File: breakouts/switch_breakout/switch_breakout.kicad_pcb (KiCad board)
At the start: 2 copper layers, 11 parts, among them P1 CONN_01X03, U1 CONN_SMA, U2 CONN_SMA, U3 PE42521, U4 CONN_SMA, U5 mounting_box

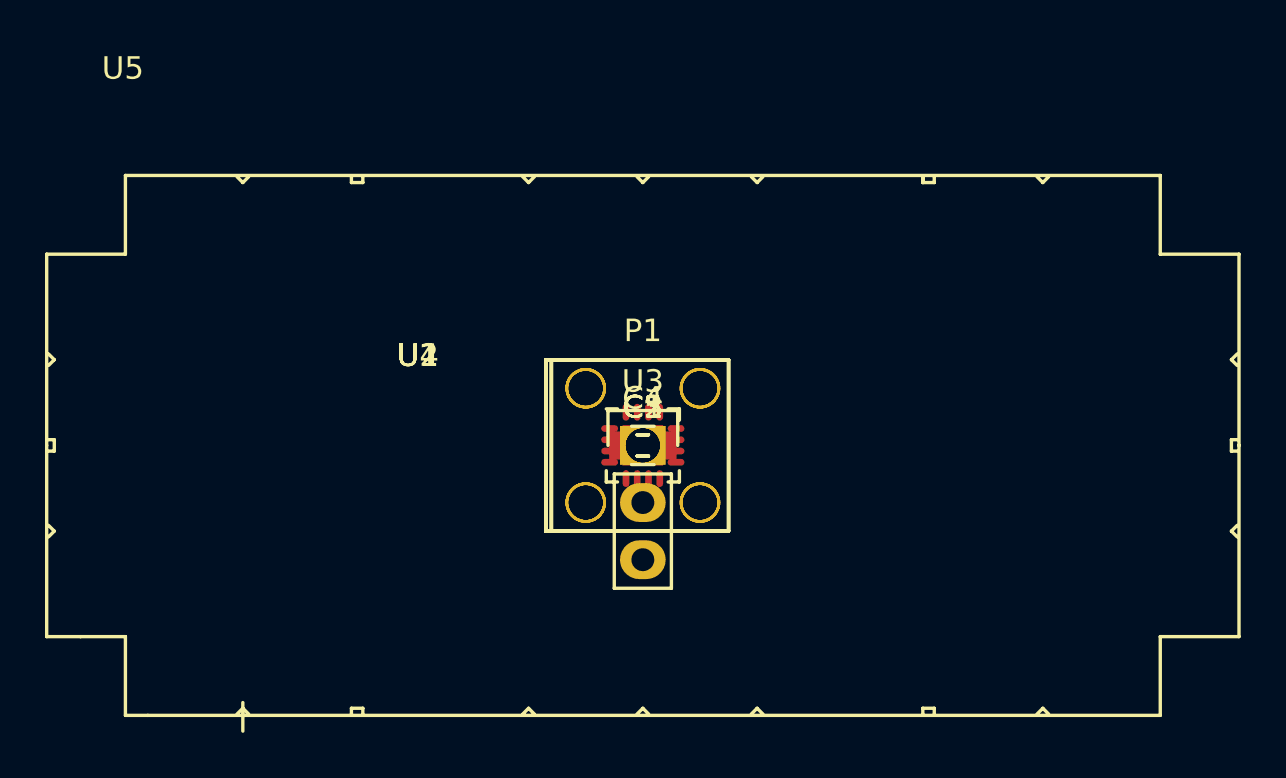
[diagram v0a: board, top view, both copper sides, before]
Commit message: layout of splitter, switch, and filter
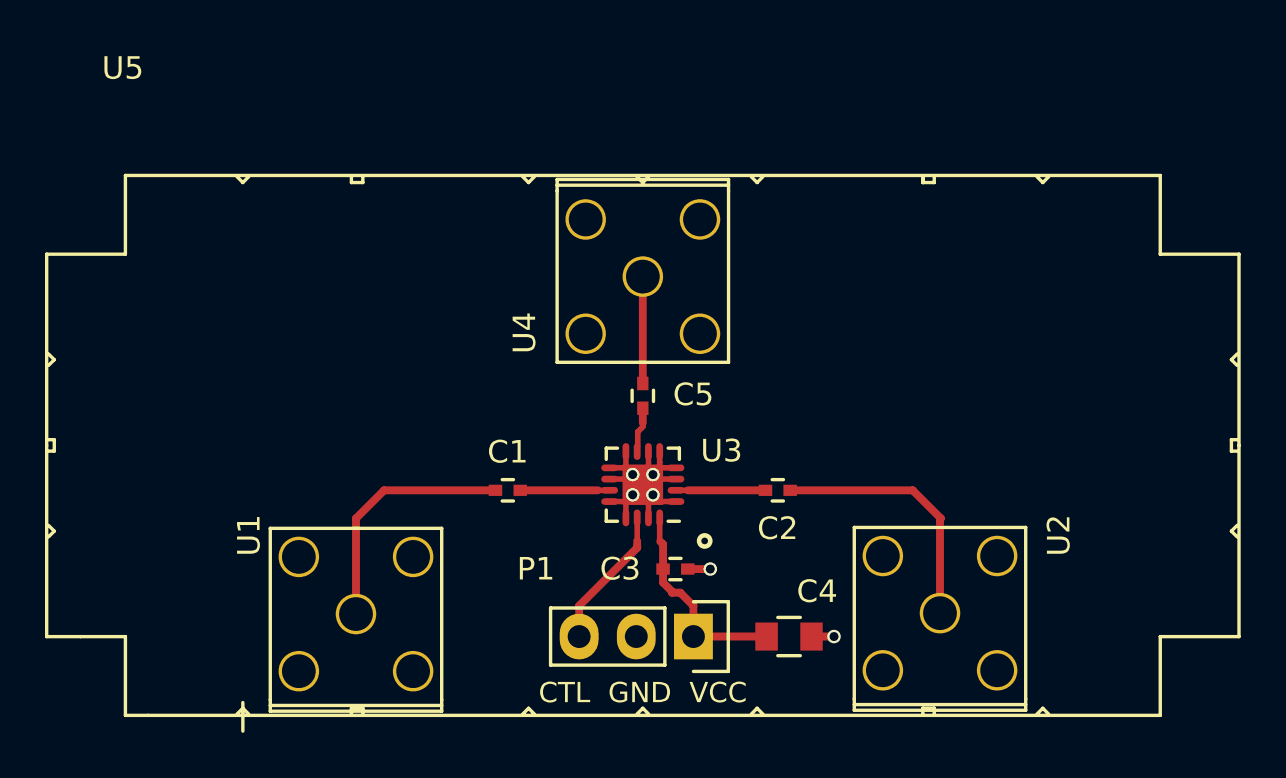
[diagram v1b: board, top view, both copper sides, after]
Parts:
- moved U2 15.2 mm to (161.7, 112.5), turned to 90 degrees
- moved U1 14.8 mm to (135.8, 112.5), turned to 90 degrees
- moved C4 10.7 mm to (155.0, 113.5)
- moved P1 8.79 mm to (150.8, 113.5), turned to 270 degrees
- moved U4 7.50 mm to (148.5, 97.5), turned to 270 degrees
- moved C1 6.32 mm to (142.5, 107.0)
- moved C2 6.32 mm to (154.5, 107.0), turned to 180 degrees
- moved C3 5.68 mm to (149.9, 110.5)
- moved C5 2.20 mm to (148.5, 102.8), turned to 270 degrees
- moved U3 1.75 mm to (148.5, 106.8), turned to 180 degrees
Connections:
- U3 pad 17: Net-(U3-Pad17) -> GND
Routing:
- net GND: track 0.00 -> 13.6 mm, vias 0 -> 6
- net Net-(C2-Pad1): track 0.00 -> 11.4 mm
- net Net-(C1-Pad1): track 0.00 -> 11.0 mm
- net Net-(C3-Pad1): track 0.00 -> 9.36 mm
- net Net-(P1-Pad3): track 0.00 -> 6.50 mm
- net Net-(C5-Pad1): track 0.00 -> 4.75 mm
- net Net-(C2-Pad2): track 0.00 -> 3.97 mm
- net Net-(C1-Pad2): track 0.00 -> 3.97 mm
- net Net-(C5-Pad2): track 0.00 -> 1.77 mm
- added copper zone on In1.Cu, net GND
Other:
- copper layers 2 -> 4
- board text added: "CTL GND VCC"

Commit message: started variable attenuator, revised synth, and added power splittert to detect board
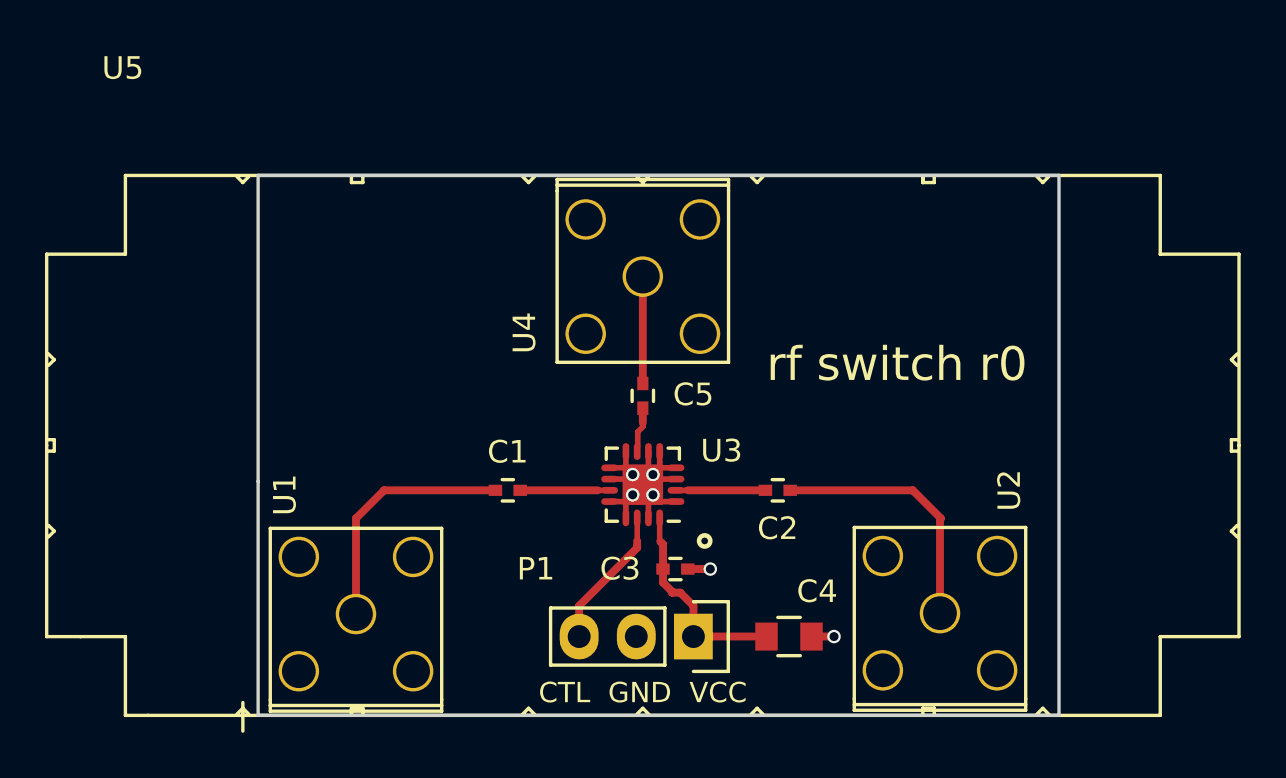
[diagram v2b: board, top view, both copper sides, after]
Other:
- board outline added: 35.6 x 24 mm
- board text added: "2016.03"
- board text added: "rf switch r0"
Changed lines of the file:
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@@
   (general
     (links 39)
-    (no_connects 39)
-    (area 0 0 0 0)
+    (no_connects 0)
+    (area 117.25 85.8446 178.250001 122.703571)
     (thickness 1.6)
-    (drawings 2)
+    (drawings 9)
     (tracks 63)
     (zones 0)
@@
   )
   (setup
-    (last_trace_width 0.35)
+    (last_trace_width 0.25)
     (user_trace_width 0.35)
     (trace_clearance 0.2)
@@
     (visible_elements FFFEFF7F)
     (pcbplotparams
-      (layerselection 0x00030_80000001)
+      (layerselection 0x010f0_80000007)
       (usegerberextensions false)
       (excludeedgelayer true)
@@
       (outputformat 1)
       (mirror false)
-      (drillshape 1)
+      (drillshape 0)
       (scaleselection 1)
-      (outputdirectory ""))
+      (outputdirectory gerbs/))
   )
   (net 0 "")
@@
   (module vna_footprints:732512200_SMA (layer F.Cu)
     (at 135.75 112.5 90)
-    (fp_text reference U1 (at 3.5 -4.75 90) (layer F.SilkS)
+    (fp_text reference U1 (at 5.3 -3.15 90) (layer F.SilkS)
       (effects (font (size 1 1) (thickness 0.15)))
     )
@@
   (module vna_footprints:732512200_SMA (layer F.Cu)
     (at 161.71 112.46 90)
-    (fp_text reference U2 (at 3.46 5.29 90) (layer F.SilkS)
+    (fp_text reference U2 (at 5.46 3.09 90) (layer F.SilkS)
       (effects (font (size 1 1) (thickness 0.15)))
     )
@@
       (net 6 GND))
   )
+  (gr_text "rf switch r0" (at 159.8 101.4) (layer F.SilkS)
+    (effects (font (size 1.5 1.5) (thickness 0.3)))
+  )
+  (gr_text 2016.03 (at 160 97) (layer B.SilkS)
+    (effects (font (size 1.5 1.5) (thickness 0.3)) (justify mirror))
+  )
+  (gr_line (start 167 117) (end 131.4 117) (layer Edge.Cuts) (width 0.15))
+  (gr_line (start 167 93) (end 167 117) (layer Edge.Cuts) (width 0.15))
+  (gr_line (start 131.4 93) (end 167 93) (layer Edge.Cuts) (width 0.15))
+  (gr_line (start 131.4 106.6) (end 131.4 93) (layer Edge.Cuts) (width 0.15))
+  (gr_line (start 131.4 117) (end 131.4 106.6) (layer Edge.Cuts) (width 0.15))
   (gr_text "CTL  GND  VCC" (at 148.5 116) (layer F.SilkS)
     (effects (font (size 0.9 0.9) (thickness 0.225)))

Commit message: trimmed ground plane on some breakouts so it doesn't disappear during panelization..
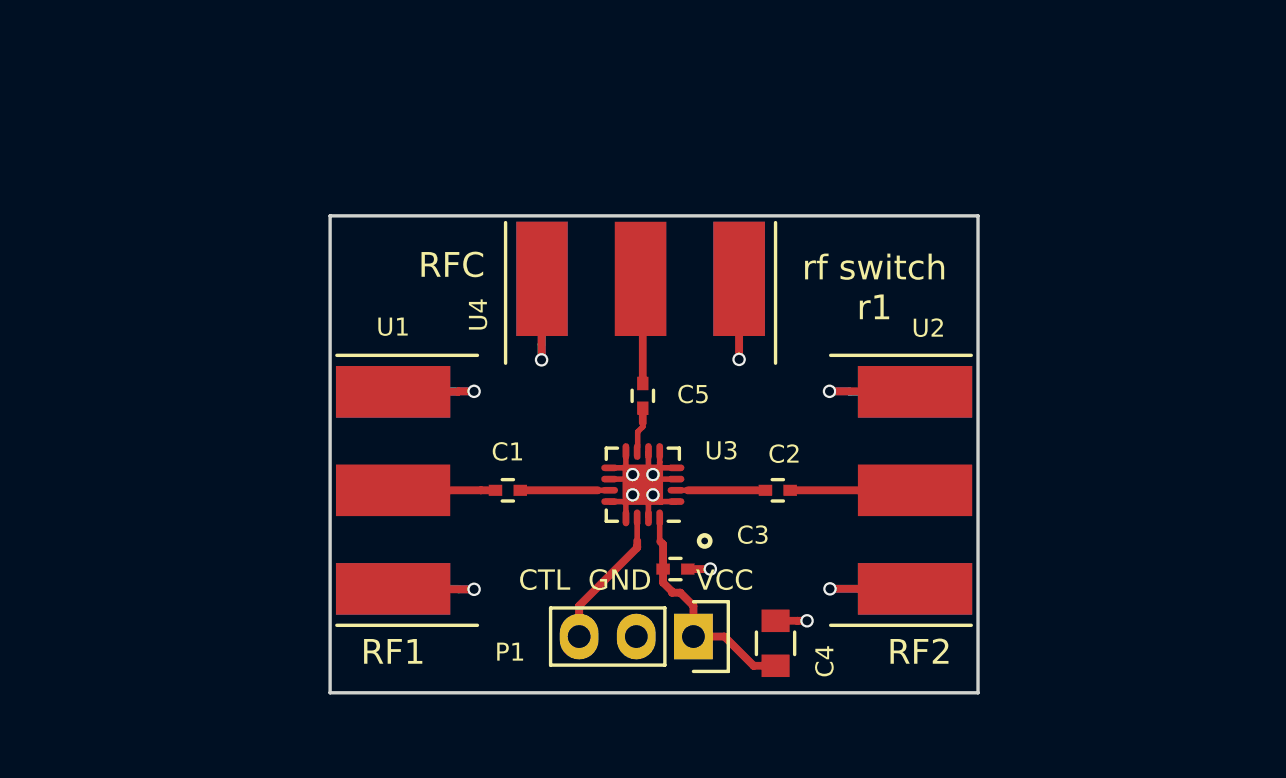
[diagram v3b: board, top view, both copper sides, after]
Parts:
- removed U5: mounting_box, vna_footprints:POMONA_2400BOX
- C1, C2, C3, C5: value C_Small -> 100 pF
- C4: value C_Small -> 10 uF
- U1, U2, U4: footprint vna_footprints:732512200_SMA -> vna_footprints:732511150_sma
- moved U1 5.74 mm to (137.4, 107.0), turned to 270 degrees
- moved U2 5.57 mm to (160.6, 107.0)
- moved C4 0.67 mm to (154.4, 113.8), turned to 90 degrees
- moved U4 0.14 mm to (148.4, 97.6), turned to 180 degrees
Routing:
- net GND: track 13.6 -> 54.4 mm, vias 6 -> 12
- net Net-(C1-Pad1): track 11.0 -> 4.55 mm
- net Net-(C2-Pad1): track 11.4 -> 5.55 mm
- net Net-(C3-Pad1): track 9.36 -> 10.3 mm
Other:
- board size 35.6 x 24 mm -> 28.8 x 21.2 mm
- board text added: "2016.04"
- board text added: "RF1"
- board text added: "RF2"
- board text added: "RFC"
- board text added: "rf switch r1"
- board text removed: "2016.03"
- board text removed: "rf switch r0"

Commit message: finished bias module, modified mixer, splitter, and switch sma connector footprints
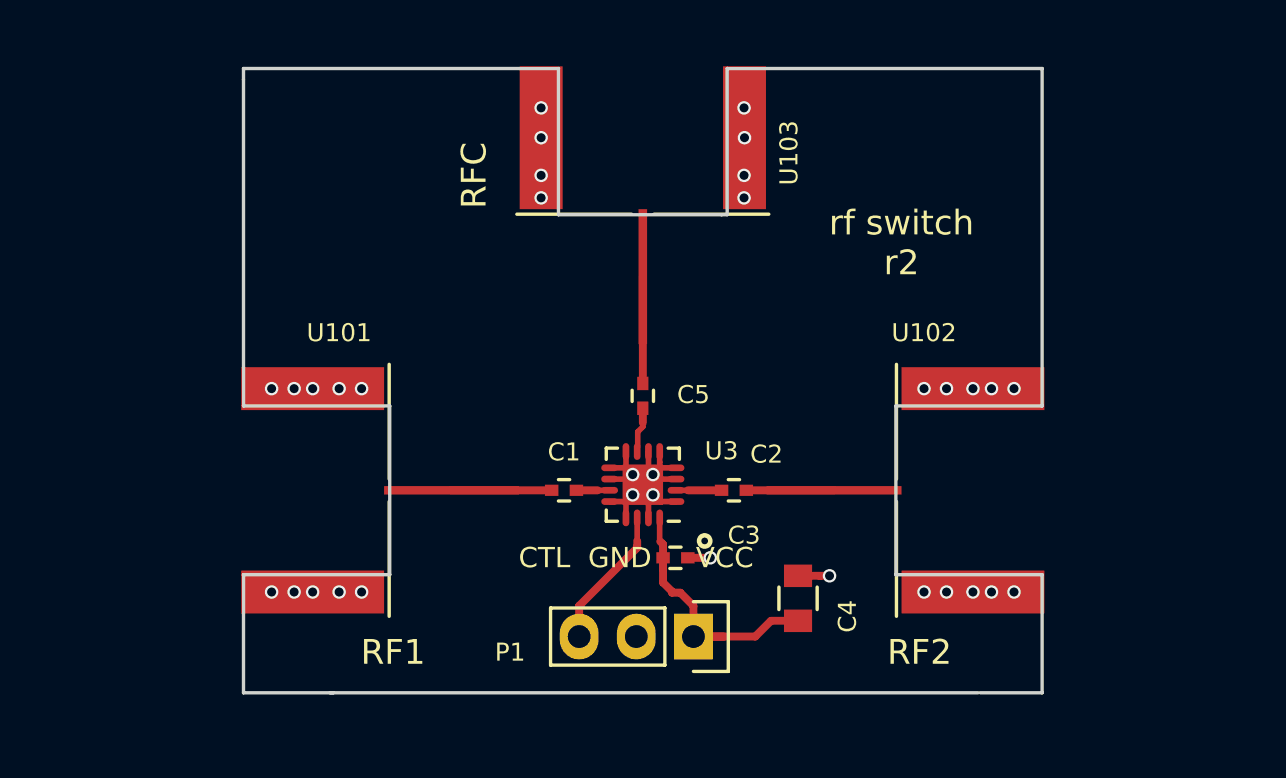
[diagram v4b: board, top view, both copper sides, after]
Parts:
- removed U1, U2, U4: CONN_SMA, vna_footprints:732511150_sma
- added U101: CONN_SMA_2GND, vna_footprints:142-0721-882_sma_cutout, F.Cu at (133.8, 107.0)
- added U102: CONN_SMA_2GND, vna_footprints:142-0721-882_sma_cutout, F.Cu at (163.2, 107.0)
- added U103: CONN_SMA_2GND, vna_footprints:142-0721-882_sma_cutout, F.Cu at (148.5, 91.3)
- moved C1 2.50 mm to (145.0, 107.0)
- moved C4 2.24 mm to (155.4, 111.8)
- moved C2 1.95 mm to (152.6, 107.0)
- moved C3 0.50 mm to (149.9, 110.0)
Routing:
- net GND: track 54.4 -> 14.0 mm, vias 12 -> 34
- net Net-(C3-Pad1): track 10.3 -> 12.9 mm
- net Net-(C1-Pad2): track 3.97 -> 1.47 mm
- net Net-(C2-Pad2): track 3.97 -> 2.03 mm
- net Net-(C2-Pad1): track 5.55 -> 4.10 mm
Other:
- board size 28.8 x 21.2 mm -> 35.5 x 27.8 mm
- net class Default: clearance 0.2 -> 0.127
- rule trace_clearance: 0.2 -> 0.127
- board text added: "rf switch r2"
- board text removed: "rf switch r1"
